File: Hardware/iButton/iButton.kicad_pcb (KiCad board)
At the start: 2 copper layers, 15.8 x 24.3 mm, 29 parts, among them IC1 TSOP75338TR, J1 Conn_01x06, X1b1 PG-2.5-9.5-SM, X2b1 PG-2.5-8.0-SM, X3b1 PG-3.0-10.0-SM

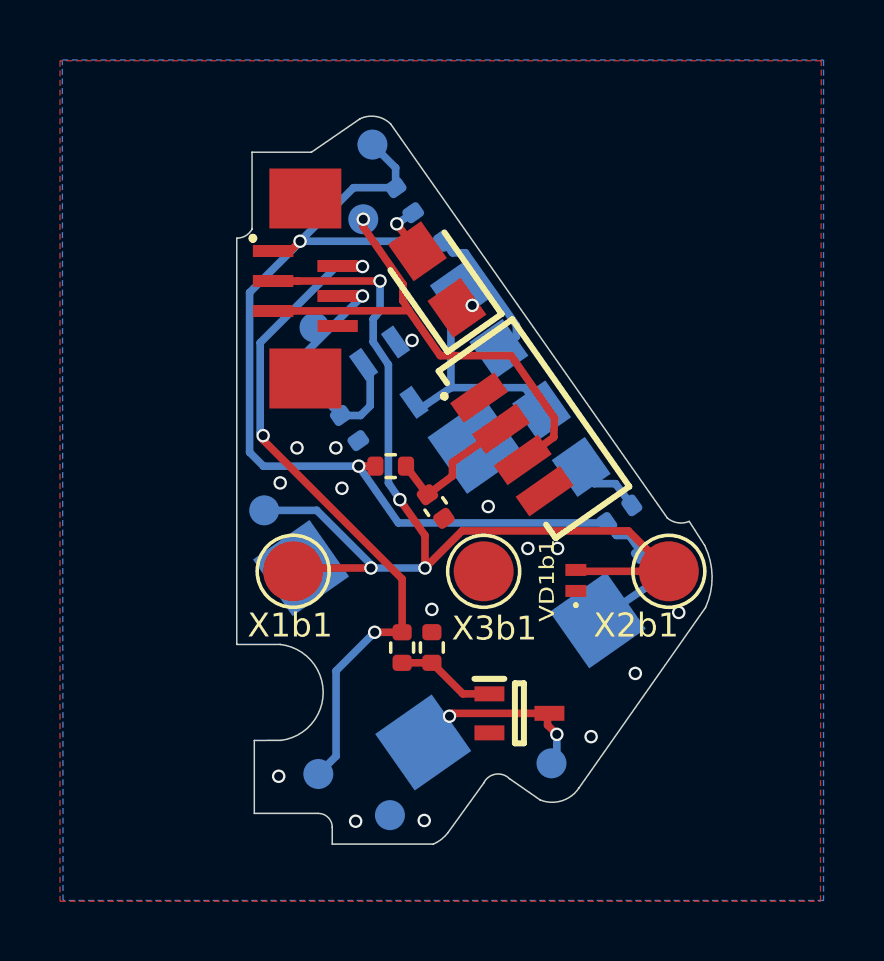
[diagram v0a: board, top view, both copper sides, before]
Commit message: PCB: iButton Fix missing hole
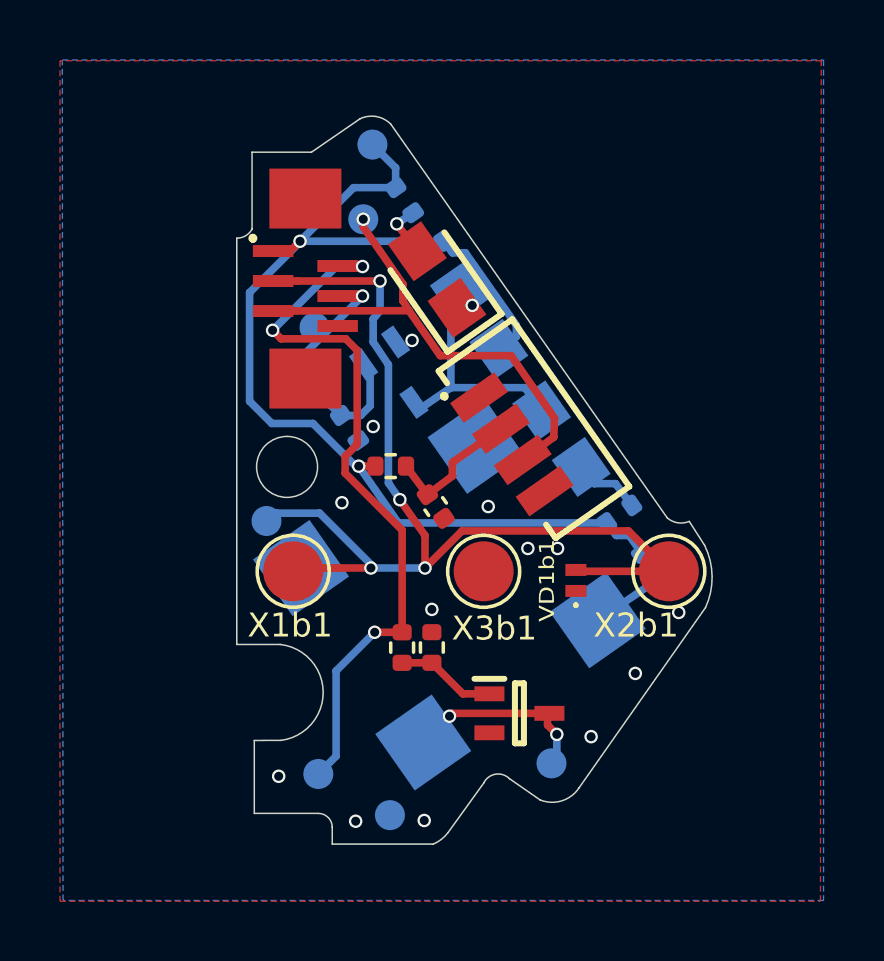
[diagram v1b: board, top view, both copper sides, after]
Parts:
- moved iButton1 0.36 mm to (159.2, 99.1)
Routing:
- net /SPEAKER: track 23.3 -> 24.6 mm
- net SYS: track 34.1 -> 33.1 mm
- net GND: vias 15 -> 13
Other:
- outline, holes or cut-outs redrawn
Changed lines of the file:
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@@
 	(footprint "TestPoint:TestPoint_Pad_D1.0mm"
 		(layer "B.Cu")
-		(at 159.1564 98.7298 180)
+		(at 159.2326 99.0854 180)
 		(descr "SMD pad as test Point, diameter 1.0mm")
 		(tags "test point SMD pad")
 		(property "Reference" "iButton1"
-			(at -0.635 1.4986 180)
+			(at -1.8796 0.8382 -155)
 			(layer "B.SilkS")
 			(effects
@@
 		)
 		(fp_line
-			(start -5.7 -5.7)
-			(end 5.7 -5.7)
+			(start -4.725 -4.725)
+			(end 4.675 -4.725)
 			(stroke
 				(width 0.1)
@@
 		)
 		(fp_line
-			(start -5.7 6.65)
-			(end -5.7 -5.7)
+			(start -4.725 4.674999)
+			(end -4.725 -4.725)
 			(stroke
 				(width 0.1)
@@
 		)
 		(fp_line
-			(start 5.7 -5.7)
-			(end 5.7 6.65)
+			(start 4.675 -4.725)
+			(end 4.675 4.675)
 			(stroke
 				(width 0.1)
@@
 		)
 		(fp_line
-			(start 5.7 6.65)
-			(end -5.7 6.65)
+			(start 4.675 4.675)
+			(end -4.725 4.674999)
 			(stroke
 				(width 0.1)
@@
 		(layer "Edge.Cuts")
 	)
+	(gr_circle
+		(center 159.9184 97.282)
+		(end 160.9344 97.2566)
+		(stroke
+			(width 0.05)
+			(type default)
+		)
+		(fill none)
+		(layer "Edge.Cuts")
+	)
 	(gr_rect
 		(start 158.496 85.5726)
@@
 	)
 	(segment
-		(start 160.909 98.7298)
-		(end 159.1564 98.7298)
-		(width 0.254)
-		(layer "B.Cu")
-		(net 3)
-	)
-	(segment
 		(start 162.7886 92.3544)
 		(end 163.0172 92.075)
@@
 	)
 	(segment
+		(start 161.002569 98.823369)
+		(end 159.570831 98.823369)
+		(width 0.254)
+		(layer "B.Cu")
+		(net 3)
+	)
+	(segment
+		(start 159.570831 98.823369)
+		(end 159.258 99.1362)
+		(width 0.254)
+		(layer "B.Cu")
+		(net 3)
+	)
+	(segment
 		(start 162.7124 100.5332)
-		(end 160.909 98.7298)
+		(end 161.002569 98.823369)
 		(width 0.254)
 		(layer "B.Cu")
@@
 	)
 	(via
-		(at 161.544 96.647)
+		(at 162.7886 95.9358)
 		(size 0.45)
 		(drill 0.3)
@@
 	)
 	(via
-		(at 159.6898 97.8154)
+		(at 168.9354 99.9998)
 		(size 0.45)
 		(drill 0.3)
@@
 	)
 	(via
-		(at 161.7472 97.9932)
-		(size 0.45)
-		(drill 0.3)
-		(layers "F.Cu" "B.Cu")
-		(free yes)
-		(net 4)
-	)
-	(via
-		(at 168.9354 99.9998)
+		(at 161.7472 98.4758)
 		(size 0.45)
 		(drill 0.3)
@@
 	)
 	(via
-		(at 160.2486 96.647)
-		(size 0.45)
-		(drill 0.3)
-		(layers "F.Cu" "B.Cu")
-		(free yes)
-		(net 4)
-	)
-	(via
 		(at 164.4904 109.0676)
 		(size 0.45)
@@
 	)
 	(segment
-		(start 160.3502 89.789)
-		(end 160.3502 89.760602)
+		(start 170.8912 99.568)
+		(end 170.575032 99.149324)
 		(width 0.254)
 		(layer "B.Cu")
@@
 	)
 	(segment
-		(start 170.8912 99.568)
-		(end 170.575032 99.149324)
+		(start 171.817876 100.242432)
+		(end 171.66814 100.242432)
 		(width 0.254)
 		(layer "B.Cu")
@@
 	)
 	(segment
-		(start 159.131 97.2566)
-		(end 158.66872 96.79432)
+		(start 158.66872 95.09252)
+		(end 158.66872 91.47048)
 		(width 0.254)
 		(layer "B.Cu")
@@
 	)
 	(segment
-		(start 171.817876 100.242432)
-		(end 171.66814 100.242432)
+		(start 160.782 95.8342)
+		(end 159.4104 95.8342)
 		(width 0.254)
 		(layer "B.Cu")
@@
 	)
 	(segment
-		(start 162.306 97.2566)
-		(end 159.131 97.2566)
+		(start 171.741676 100.166232)
+		(end 171.323 99.568)
 		(width 0.254)
 		(layer "B.Cu")
@@
 	)
 	(segment
-		(start 158.66872 96.79432)
-		(end 158.66872 91.47048)
+		(start 162.306 97.2566)
+		(end 162.2044 97.2566)
 		(width 0.254)
 		(layer "B.Cu")
@@
 	)
 	(segment
-		(start 171.741676 100.166232)
-		(end 171.323 99.568)
+		(start 162.13657 87.974232)
+		(end 163.537476 87.974232)
 		(width 0.254)
 		(layer "B.Cu")
@@
 	)
 	(segment
-		(start 162.13657 87.974232)
-		(end 163.537476 87.974232)
+		(start 158.66872 91.47048)
+		(end 160.3502 89.789)
 		(width 0.254)
 		(layer "B.Cu")
@@
 	)
 	(segment
-		(start 158.66872 91.47048)
-		(end 160.3502 89.789)
+		(start 160.3502 89.789)
+		(end 160.3502 89.760602)
 		(width 0.254)
 		(layer "B.Cu")
@@
 	)
 	(segment
+		(start 159.4104 95.8342)
+		(end 158.66872 95.09252)
+		(width 0.254)
+		(layer "B.Cu")
+		(net 8)
+	)
+	(segment
 		(start 171.323 99.568)
 		(end 170.8912 99.568)
@@
 	)
 	(segment
-		(start 159.12072 96.2406)
-		(end 159.12072 96.38272)
+		(start 162.2044 97.2566)
+		(end 160.782 95.8342)
+		(width 0.254)
+		(layer "B.Cu")
+		(net 8)
+	)
+	(segment
+		(start 162.2552 96.5327)
+		(end 161.854 96.9339)
+		(width 0.254)
+		(layer "F.Cu")
+		(net 9)
+	)
+	(segment
+		(start 161.872 93.0126)
+		(end 162.2552 93.3958)
+		(width 0.254)
+		(layer "F.Cu")
+		(net 9)
+	)
+	(segment
+		(start 159.719754 93.0126)
+		(end 161.872 93.0126)
+		(width 0.254)
+		(layer "F.Cu")
+		(net 9)
+	)
+	(segment
+		(start 161.854 97.4904)
+		(end 163.7538 99.3902)
+		(width 0.254)
+		(layer "F.Cu")
+		(net 9)
+	)
+	(segment
+		(start 163.7538 99.3902)
+		(end 163.7538 102.7938)
+		(width 0.254)
+		(layer "F.Cu")
+		(net 9)
+	)
+	(segment
+		(start 161.854 96.9339)
+		(end 161.854 97.4904)
 		(width 0.254)
 		(layer "F.Cu")
@@
 	)
 	(segment
-		(start 163.7538 101.0158)
-		(end 163.7538 102.7938)
+		(start 162.2552 93.3958)
+		(end 162.2552 96.5327)
 		(width 0.254)
 		(layer "F.Cu")
@@
 	)
 	(segment
-		(start 159.12072 96.38272)
-		(end 163.7538 101.0158)
+		(start 159.4358 92.728646)
+		(end 159.719754 93.0126)
 		(width 0.254)
 		(layer "F.Cu")
@@
 	)
 	(via
-		(at 162.433 90.6018)
+		(at 159.4358 92.728646)
 		(size 0.45)
 		(drill 0.3)
@@
 	)
 	(via
-		(at 159.12072 96.2406)
+		(at 162.433 90.6018)
 		(size 0.45)
 		(drill 0.3)
@@
 	)
 	(segment
-		(start 159.02272 93.141726)
-		(end 159.02272 96.1426)
-		(width 0.254)
-		(layer "B.Cu")
-		(net 9)
-	)
-	(segment
-		(start 162.433 90.6018)
+		(start 159.4358 92.728646)
 		(end 161.562646 90.6018)
 		(width 0.254)
@@
 	)
 	(segment
-		(start 161.552508 106.925492)
-		(end 161.552508 104.080692)
+		(start 161.562646 90.6018)
+		(end 162.433 90.6018)
 		(width 0.254)
 		(layer "B.Cu")
@@
 	)
 	(segment
-		(start 161.562646 90.6018)
-		(end 159.02272 93.141726)
+		(start 161.552508 106.925492)
+		(end 161.552508 104.080692)
 		(width 0.254)
 		(layer "B.Cu")
@@
 	)
 	(segment
-		(start 159.02272 96.1426)
-		(end 159.12072 96.2406)
+		(start 159.403646 92.7608)
+		(end 159.4358 92.728646)
 		(width 0.254)
 		(layer "B.Cu")
